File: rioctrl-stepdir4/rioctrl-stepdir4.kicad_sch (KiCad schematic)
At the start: 0 parts

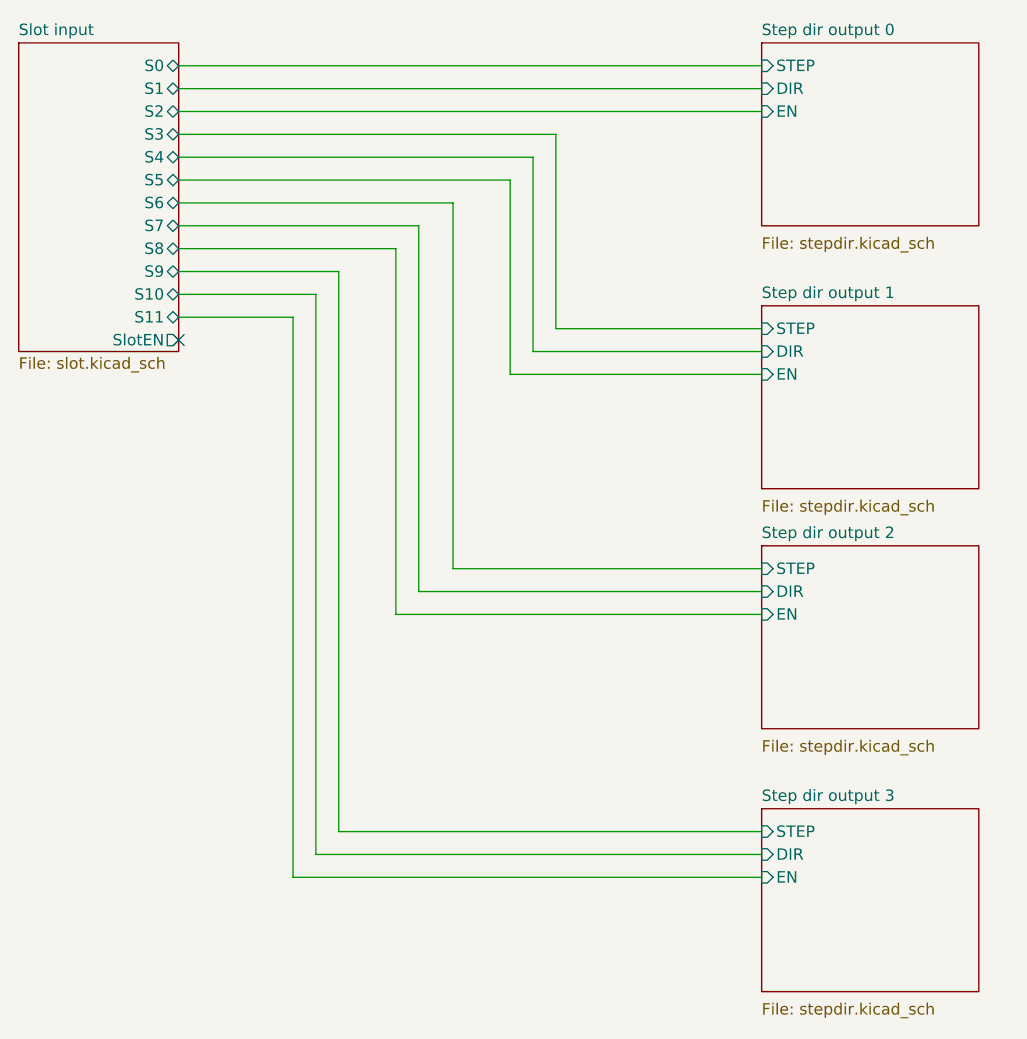
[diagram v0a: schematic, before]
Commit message: Label axes on stepdir
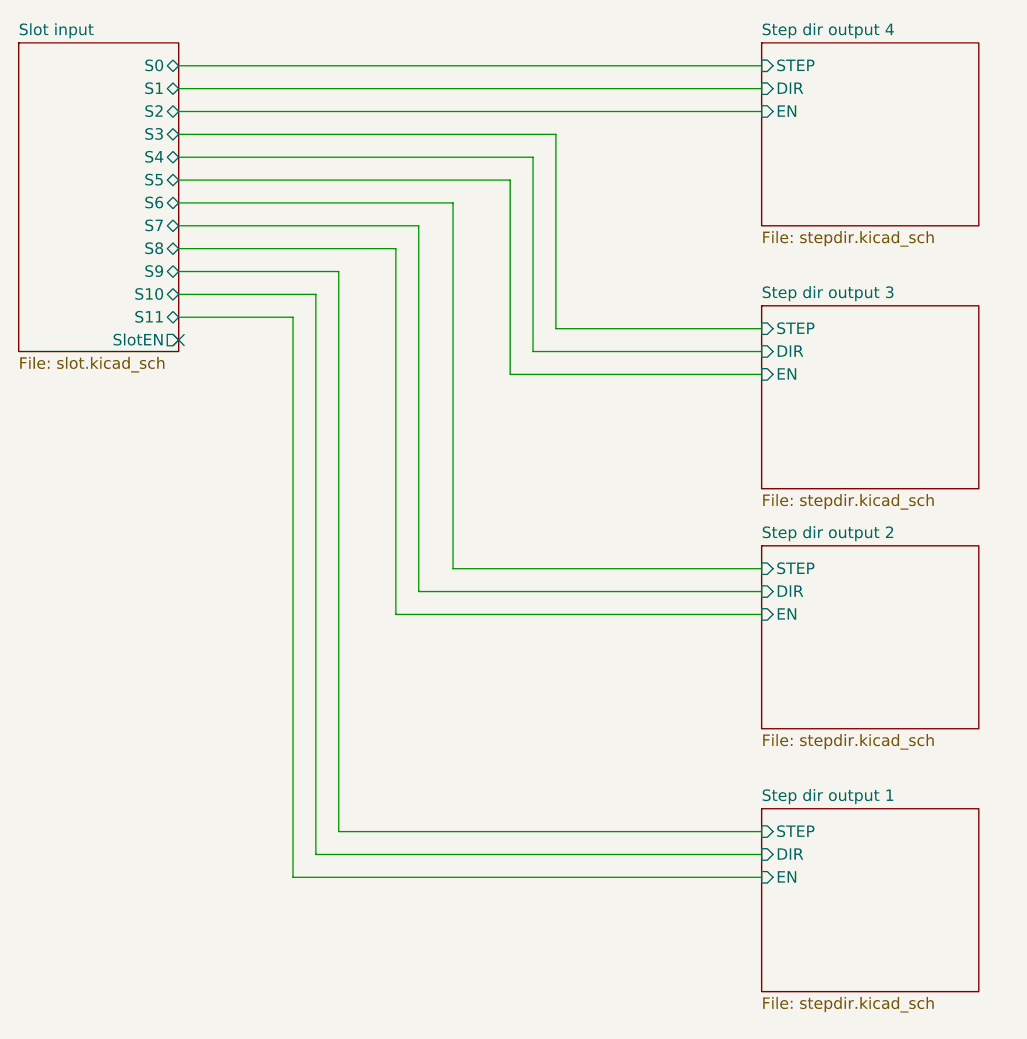
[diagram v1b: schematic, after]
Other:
- sheet Step dir output 0 renamed Step dir output 4
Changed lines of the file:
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@@
 		)
 		(property "Sheetfile" "stepdir.kicad_sch"
-			(at 105.41 106.6296 0)
+			(at 105.41 105.9946 0)
 			(effects
 				(font
@@
 			(color 0 0 0 0.0000)
 		)
-		(property "Sheetname" "Step dir output 3"
+		(property "Sheetname" "Step dir output 1"
 			(at 105.41 113.5884 0)
 			(effects
@@
 		)
 		(property "Sheetfile" "stepdir.kicad_sch"
-			(at 105.41 135.8396 0)
+			(at 105.41 135.2046 0)
 			(effects
 				(font
@@
 			(color 0 0 0 0.0000)
 		)
-		(property "Sheetname" "Step dir output 1"
+		(property "Sheetname" "Step dir output 3"
 			(at 105.41 57.7084 0)
 			(effects
@@
 		)
 		(property "Sheetfile" "stepdir.kicad_sch"
-			(at 105.41 79.9596 0)
+			(at 105.41 79.3246 0)
 			(effects
 				(font
@@
 			(color 0 0 0 0.0000)
 		)
-		(property "Sheetname" "Step dir output 0"
+		(property "Sheetname" "Step dir output 4"
 			(at 105.41 28.4984 0)
 			(effects
@@
 		)
 		(property "Sheetfile" "stepdir.kicad_sch"
-			(at 105.41 50.7496 0)
-			(effects
-				(font
+			(at 105.41 50.1146 0)
+			(effects
+				(font

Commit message: Fix ERC, add title information to sch, add initial version of build scripts
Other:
- company: (none) -> R. Veips
- title: (none) -> rioctrl-stepdir4
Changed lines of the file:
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@@
 	(generator_version "8.0")
 	(paper "A4")
+	(title_block
+		(title "rioctrl-stepdir4")
+		(date "2024-08-25")
+		(rev "${VERSION}")
+		(company "R. Veips")
+	)
 	(no_connect
 		(at 40.64 62.23)
